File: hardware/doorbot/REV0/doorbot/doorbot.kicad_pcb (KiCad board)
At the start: 2 copper layers, 65 x 56.5 mm, 78 parts, among them J1 Raspberry_Pi_2_3, J2 Screw_Terminal_01x12, J3 PoE Passthrough, J4 Conn_01x04, J5 Conn_01x04, Q1 2N7002, U1 ATmega328P-AU, U10 TLP291, U2 TLP291, U3 TLP291, U4 TLP291, U5 TLP291, U6 TLP291, U7 DRV103, U8 MC78L05_SOT89, U9 TLP291, Y1 16MHz

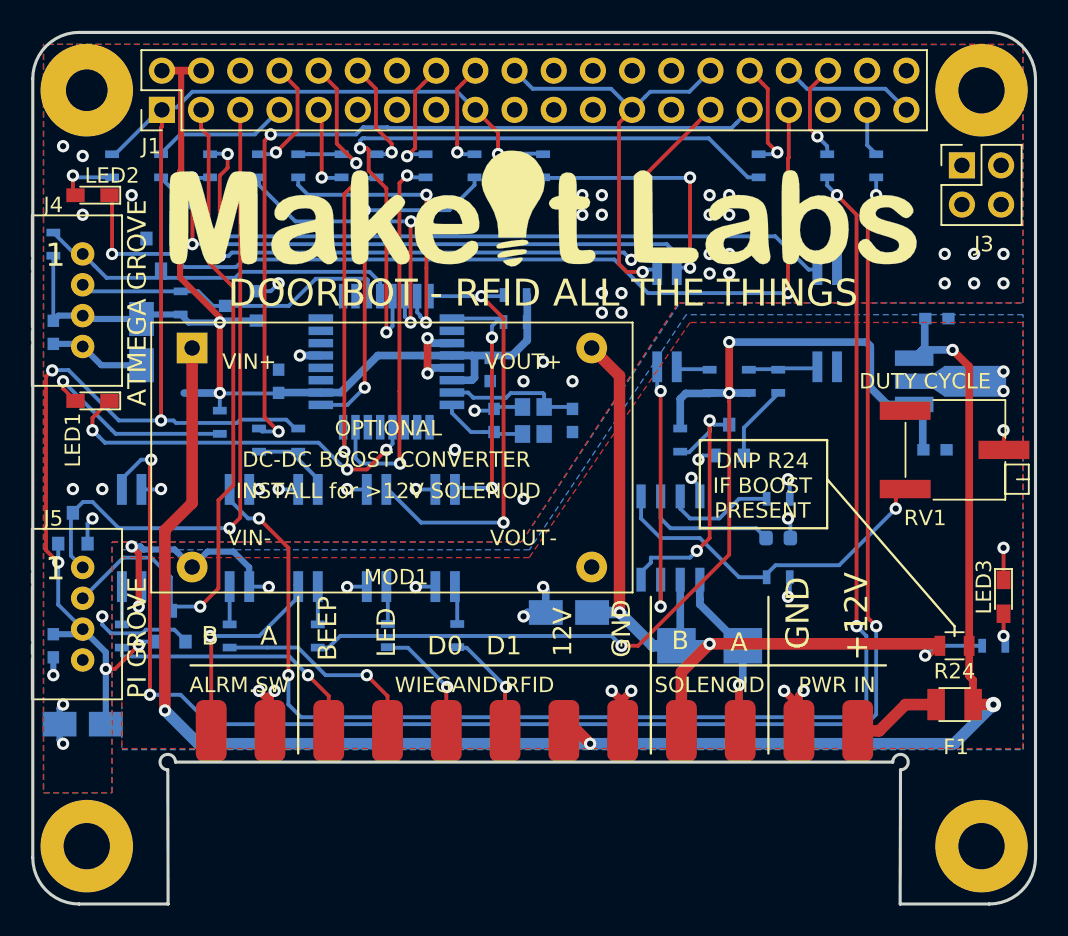
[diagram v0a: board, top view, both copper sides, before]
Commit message: move duty cycle pot, try to fix mickey mouse corners on cutout
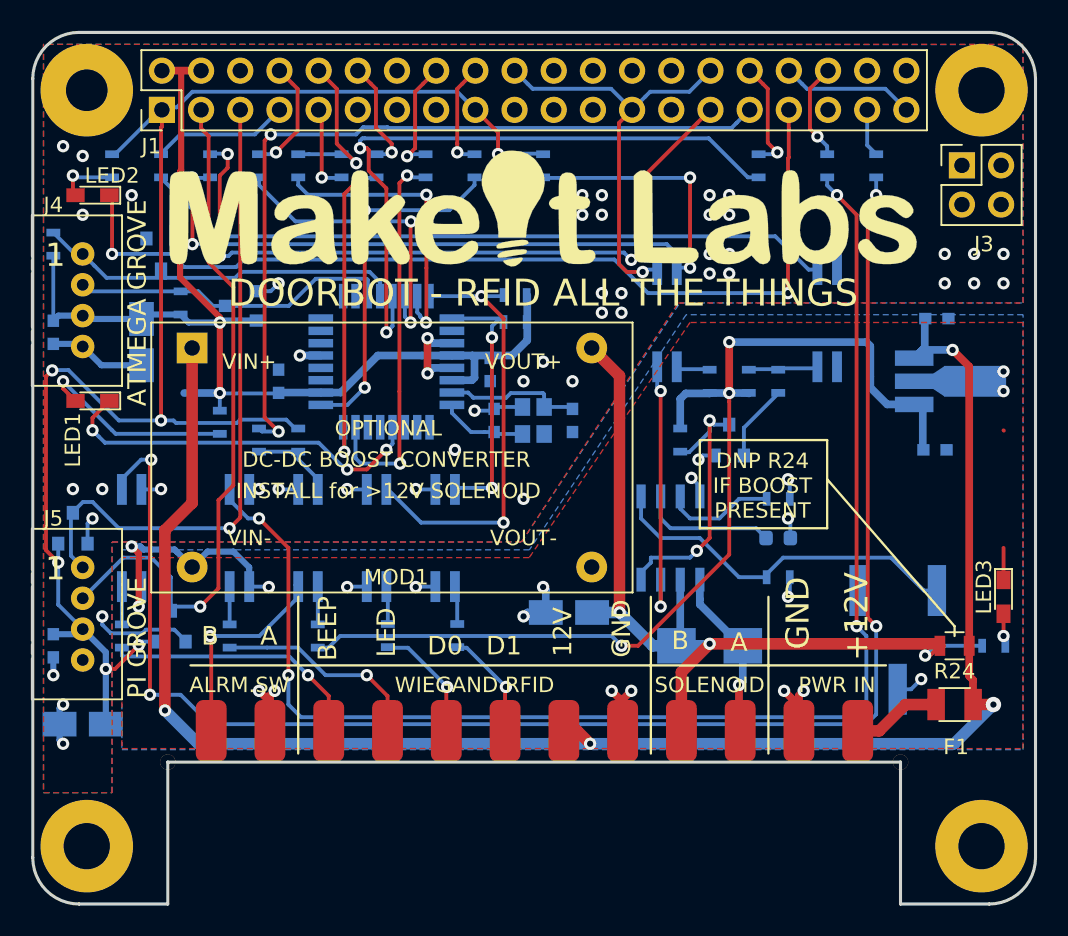
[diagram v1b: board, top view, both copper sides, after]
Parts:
- added REF**: MICKEY_MOUSE_HOLE, doorbot_pcb_library:MICKEY_MOUSE_HOLE, F.Cu at (162.2, 109.8)
- added REF**: MICKEY_MOUSE_HOLE, doorbot_pcb_library:MICKEY_MOUSE_HOLE, F.Cu at (114.7, 109.8)
- RV1: moved to B.Cu
- moved RV1 12.9 mm to (162.1, 101.9), turned to 90 degrees
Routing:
- net Net-(R13-Pad1): track 23.0 -> 23.7 mm, vias 1 -> 0
- net Earth: track 49.8 -> 50.3 mm, vias 22 -> 21
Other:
- outline, holes or cut-outs redrawn

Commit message: add atmega reset pullup & AREF cap, fix footprint library issue, small tweaks & cleanup, ready for fab
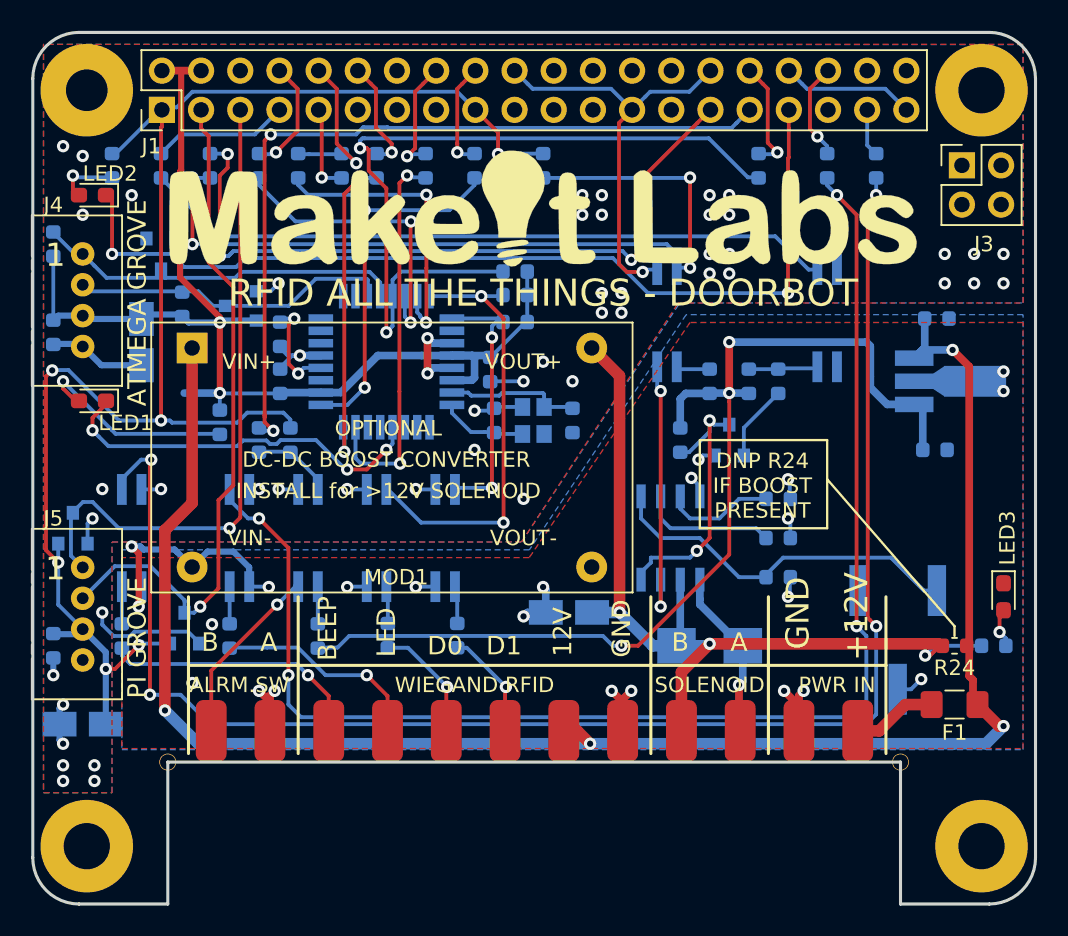
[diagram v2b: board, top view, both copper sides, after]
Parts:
- added C13: .1uF, Capacitor_SMD:C_0603_1608Metric, B.Cu at (122.0, 82.0)
- added R34: 4.7K, Resistor_SMD:R_0603_1608Metric, B.Cu at (137.2, 78.0)
- C10, C12, C3, C4, C5, C6, C7, C8: footprint Capacitors_SMD:C_0603 -> Capacitor_SMD:C_0603_1608Metric
- C11, C2, C9: footprint Capacitors_SMD:CP_Elec_3x5.3 -> Capacitor_SMD:CP_Elec_3x5.3
- D5, D6, D7, D8: footprint TO_SOT_Packages_SMD:SOT-23 -> Package_TO_SOT_SMD:SOT-23
- F1: footprint Fuse_Holders_and_Fuses:Fuse_SMD1206_Reflow -> Fuse:Fuse_1206_3216Metric_Pad1.42x1.75mm_HandSolder
- LED1, LED2, LED3: footprint LEDs:LED_0603_HandSoldering -> LED_SMD:LED_0603_1608Metric_Pad1.05x0.95mm_HandSolder
- R1, R10, R11, R12, R13, R14, R15, R16, R17, R18, R19, R2, R20, R21, R22, R23, R25, R26, R27, R28, R29, R3, R30, R31, R32, R33, R4, R5, R6, R7, R8, R9: footprint Resistors_SMD:R_0603 -> Resistor_SMD:R_0603_1608Metric
- R24: footprint Resistors_SMD:R_0805 -> Resistor_SMD:R_0603_1608Metric
- U10, U2, U3, U4, U5, U6, U9: footprint Housings_SOIC:SO-4_4.4x2.3mm_Pitch1.27mm -> Package_SO:SO-4_4.4x2.3mm_P1.27mm
- Y1: footprint Crystals:Crystal_SMD_2520-4pin_2.5x2.0mm -> Crystal:Crystal_SMD_2520-4Pin_2.5x2.0mm
- moved D7 0.90 mm to (115.8, 101.1)
- moved R10 0.51 mm to (122.7, 88.9)
- moved R33 0.13 mm to (115.7, 80.1)
- moved C6 0.10 mm to (122.0, 85.1)
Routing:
- net /AT_RST: track 42.8 -> 51.3 mm
- net GND: track 78.6 -> 85.4 mm, vias 50 -> 53
- net Net-(C13-Pad1): track 0.00 -> 6.69 mm, vias 0 -> 2
- net +5V: track 75.6 -> 77.9 mm
- net Earth: track 50.3 -> 48.2 mm, vias 21 -> 23
- net +3V3: track 102.0 -> 103.5 mm
- net PI_SDA: track 45.5 -> 44.3 mm
- net /DOOR_SWITCH_IN: track 14.0 -> 12.8 mm
- net +12VA: track 112.5 -> 113.4 mm
- net /WG_BEEP_RAW: track 17.3 -> 16.8 mm
- net Net-(LED1-Pad1): track 24.6 -> 25.1 mm
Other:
- board text added: "REV0 2019.03.23 - STEVE RICHARDSON"
- board text added: "RFID ALL THE THINGS - DOORBOT"
- board text removed: "DOORBOT - RFID ALL THE THINGS"
- board text removed: "REV0 2019.03.22 - STEVE RICHARDSON"
